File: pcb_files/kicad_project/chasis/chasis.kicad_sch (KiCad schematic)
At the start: 3 parts, among them J1 Conn_01x01_Pin, J2 Conn_01x08_Pin, J3 Conn_01x08_Pin

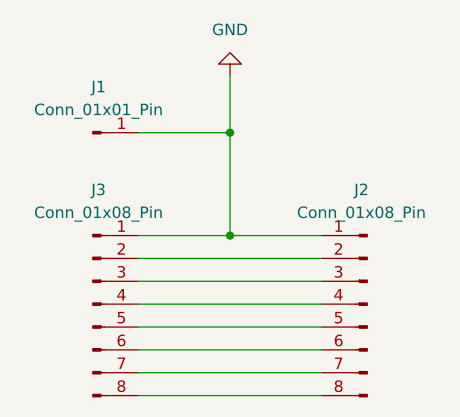
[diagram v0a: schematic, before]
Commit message: Finaliza la PCB del chasis
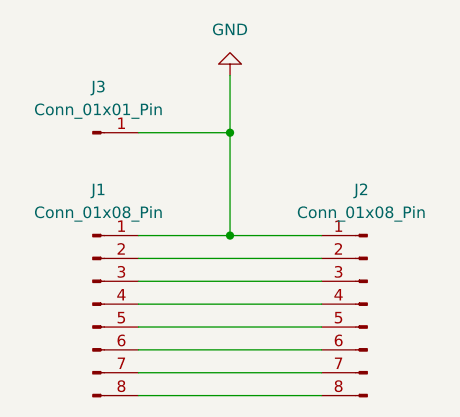
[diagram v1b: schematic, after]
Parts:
- J1: renamed from J3; footprint Connector_PinHeader_2.54mm:PinHeader_1x01_P2.54mm_Vertical -> custom_footprints:DragonBot_pads_main
- J2: footprint custom_footprints:DragonBot_pads_main -> custom_footprints:DragonBot_pads_morro
- J3: renamed from J1; footprint custom_footprints:DragonBot_pads_morro -> Connector_PinHeader_2.54mm:PinHeader_1x01_P2.54mm_Vertical
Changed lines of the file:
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@@
 (kicad_sch
-	(version 20231120)
+	(version 20260306)
 	(generator "eeschema")
-	(generator_version "8.0")
+	(generator_version "10.0")
 	(paper "A4")
 	(junction
@@
 		(mirror y)
 		(unit 1)
+		(body_style 1)
 		(exclude_from_sim no)
 		(in_bom yes)
 		(on_board yes)
+		(in_pos_files yes)
 		(dnp no)
 		(property "Reference" "J2"
 			(at 159.385 88.9 0)
+			(show_name no)
+			(do_not_autoplace no)
 			(effects
 				(font
@@
 		(property "Value" "Conn_01x08_Pin"
 			(at 159.385 91.44 0)
-			(effects
-				(font
-					(size 1.27 1.27)
-				)
-			)
-		)
-		(property "Footprint" "custom_footprints:DragonBot_pads_main"
+			(show_name no)
+			(do_not_autoplace no)
+			(effects
+				(font
+					(size 1.27 1.27)
+				)
+			)
+		)
+		(property "Footprint" "custom_footprints:DragonBot_pads_morro"
 			(at 160.02 101.6 0)
-			(effects
-				(font
-					(size 1.27 1.27)
-				)
-				(hide yes)
-			)
-		)
-		(property "Datasheet" "~"
+			(hide yes)
+			(show_name no)
+			(do_not_autoplace no)
+			(effects
+				(font
+					(size 1.27 1.27)
+				)
+			)
+		)
+		(property "Datasheet" ""
 			(at 160.02 101.6 0)
-			(effects
-				(font
-					(size 1.27 1.27)
-				)
-				(hide yes)
+			(hide yes)
+			(show_name no)
+			(do_not_autoplace no)
+			(effects
+				(font
+					(size 1.27 1.27)
+				)
 			)
 		)
 		(property "Description" "Generic connector, single row, 01x08, script generated"
 			(at 160.02 101.6 0)
-			(effects
-				(font
-					(size 1.27 1.27)
-				)
-				(hide yes)
+			(hide yes)
+			(show_name no)
+			(do_not_autoplace no)
+			(effects
+				(font
+					(size 1.27 1.27)
+				)
 			)
 		)
@@
 		(at 144.78 76.2 180)
 		(unit 1)
+		(body_style 1)
 		(exclude_from_sim no)
 		(in_bom yes)
 		(on_board yes)
+		(in_pos_files yes)
 		(dnp no)
 		(fields_autoplaced yes)
 		(property "Reference" "#PWR01"
 			(at 144.78 69.85 0)
-			(effects
-				(font
-					(size 1.27 1.27)
-				)
-				(hide yes)
+			(hide yes)
+			(show_name no)
+			(do_not_autoplace no)
+			(effects
+				(font
+					(size 1.27 1.27)
+				)
 			)
 		)
 		(property "Value" "GND"
 			(at 144.78 71.12 0)
+			(show_name no)
+			(do_not_autoplace no)
 			(effects
 				(font
@@
 		(property "Footprint" ""
 			(at 144.78 76.2 0)
-			(effects
-				(font
-					(size 1.27 1.27)
-				)
-				(hide yes)
+			(hide yes)
+			(show_name no)
+			(do_not_autoplace no)
+			(effects
+				(font
+					(size 1.27 1.27)
+				)
 			)
 		)
 		(property "Datasheet" ""
 			(at 144.78 76.2 0)
-			(effects
-				(font
-					(size 1.27 1.27)
-				)
-				(hide yes)
+			(hide yes)
+			(show_name no)
+			(do_not_autoplace no)
+			(effects
+				(font
+					(size 1.27 1.27)
+				)
 			)
 		)
 		(property "Description" "Power symbol creates a global label with name \"GND\" , ground"
 			(at 144.78 76.2 0)
-			(effects
-				(font
-					(size 1.27 1.27)
-				)
-				(hide yes)
+			(hide yes)
+			(show_name no)
+			(do_not_autoplace no)
+			(effects
+				(font
+					(size 1.27 1.27)
+				)
 			)
 		)
@@
 		)
 		(instances
-			(project ""
+			(project "chasis"
 				(path "/723c5205-0ad3-4e7d-96f4-dd689760a9b5"
 					(reference "#PWR01")
@@
 		(at 129.54 101.6 0)
 		(unit 1)
+		(body_style 1)
 		(exclude_from_sim no)
 		(in_bom yes)
 		(on_board yes)
+		(in_pos_files yes)
 		(dnp no)
 		(fields_autoplaced yes)
-		(property "Reference" "J3"
+		(property "Reference" "J1"
 			(at 130.175 88.9 0)
+			(show_name no)
+			(do_not_autoplace no)
 			(effects
 				(font
@@
 		(property "Value" "Conn_01x08_Pin"
 			(at 130.175 91.44 0)
-			(effects
-				(font
-					(size 1.27 1.27)
-				)
-			)
-		)
-		(property "Footprint" "Connector_PinHeader_2.54mm:PinHeader_1x01_P2.54mm_Vertical"
+			(show_name no)
+			(do_not_autoplace no)
+			(effects
+				(font
+					(size 1.27 1.27)
+				)
+			)
+		)
+		(property "Footprint" "custom_footprints:DragonBot_pads_main"
 			(at 129.54 101.6 0)
-			(effects
-				(font
-					(size 1.27 1.27)
-				)
-				(hide yes)
-			)
-		)
-		(property "Datasheet" "~"
+			(hide yes)
+			(show_name no)
+			(do_not_autoplace no)
+			(effects
+				(font
+					(size 1.27 1.27)
+				)
+			)
+		)
+		(property "Datasheet" ""
 			(at 129.54 101.6 0)
-			(effects
-				(font
-					(size 1.27 1.27)
-				)
-				(hide yes)
+			(hide yes)
+			(show_name no)
+			(do_not_autoplace no)
+			(effects
+				(font
+					(size 1.27 1.27)
+				)
 			)
 		)
 		(property "Description" "Generic connector, single row, 01x08, script generated"
 			(at 129.54 101.6 0)
-			(effects
-				(font
-					(size 1.27 1.27)
-				)
-				(hide yes)
+			(hide yes)
+			(show_name no)
+			(do_not_autoplace no)
+			(effects
+				(font
+					(size 1.27 1.27)
+				)
 			)
 		)
@@
 		)
 		(instances
-			(project ""
+			(project "chasis"
 				(path "/723c5205-0ad3-4e7d-96f4-dd689760a9b5"
-					(reference "J3")
+					(reference "J1")
 					(unit 1)
 				)
@@
 		(at 129.54 82.55 0)
 		(unit 1)
+		(body_style 1)
 		(exclude_from_sim no)
 		(in_bom yes)
 		(on_board yes)
+		(in_pos_files yes)
 		(dnp no)
 		(fields_autoplaced yes)
-		(property "Reference" "J1"
+		(property "Reference" "J3"
 			(at 130.175 77.47 0)
+			(show_name no)
+			(do_not_autoplace no)
 			(effects
 				(font
@@
 		(property "Value" "Conn_01x01_Pin"
 			(at 130.175 80.01 0)
-			(effects
-				(font
-					(size 1.27 1.27)
-				)
-			)
-		)
-		(property "Footprint" "custom_footprints:DragonBot_pads_morro"
+			(show_name no)
+			(do_not_autoplace no)
+			(effects
+				(font
+					(size 1.27 1.27)
+				)
+			)
+		)
+		(property "Footprint" "Connector_PinHeader_2.54mm:PinHeader_1x01_P2.54mm_Vertical"
 			(at 129.54 82.55 0)
-			(effects
-				(font
-					(size 1.27 1.27)
-				)
-				(hide yes)
-			)
-		)
-		(property "Datasheet" "~"
+			(hide yes)
+			(show_name no)
+			(do_not_autoplace no)
+			(effects
+				(font
+					(size 1.27 1.27)
+				)
+			)
+		)
+		(property "Datasheet" ""
 			(at 129.54 82.55 0)
-			(effects
-				(font
-					(size 1.27 1.27)
-				)
-				(hide yes)
+			(hide yes)
+			(show_name no)
+			(do_not_autoplace no)
+			(effects
+				(font
+					(size 1.27 1.27)
+				)
 			)
 		)
 		(property "Description" "Generic connector, single row, 01x01, script generated"
 			(at 129.54 82.55 0)
-			(effects
-				(font
-					(size 1.27 1.27)
-				)
-				(hide yes)
+			(hide yes)
+			(show_name no)
+			(do_not_autoplace no)
+			(effects
+				(font
+					(size 1.27 1.27)
+				)
 			)
 		)
@@
 		)
 		(instances
-			(project ""
+			(project "chasis"
 				(path "/723c5205-0ad3-4e7d-96f4-dd689760a9b5"
-					(reference "J1")
+					(reference "J3")
 					(unit 1)
 				)
@@
 		)
 	)
+	(embedded_fonts no)
 )
